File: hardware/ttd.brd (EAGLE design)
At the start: 100 x 80 mm, 19 parts, among them Q1 IRFZ44N, Q2 IRFZ44N, Q3 IRFZ44N, Q4 IRFZ44N, X1 MKDSN1,5/2-5,08, X2 MKDSN1,5/2-5,08

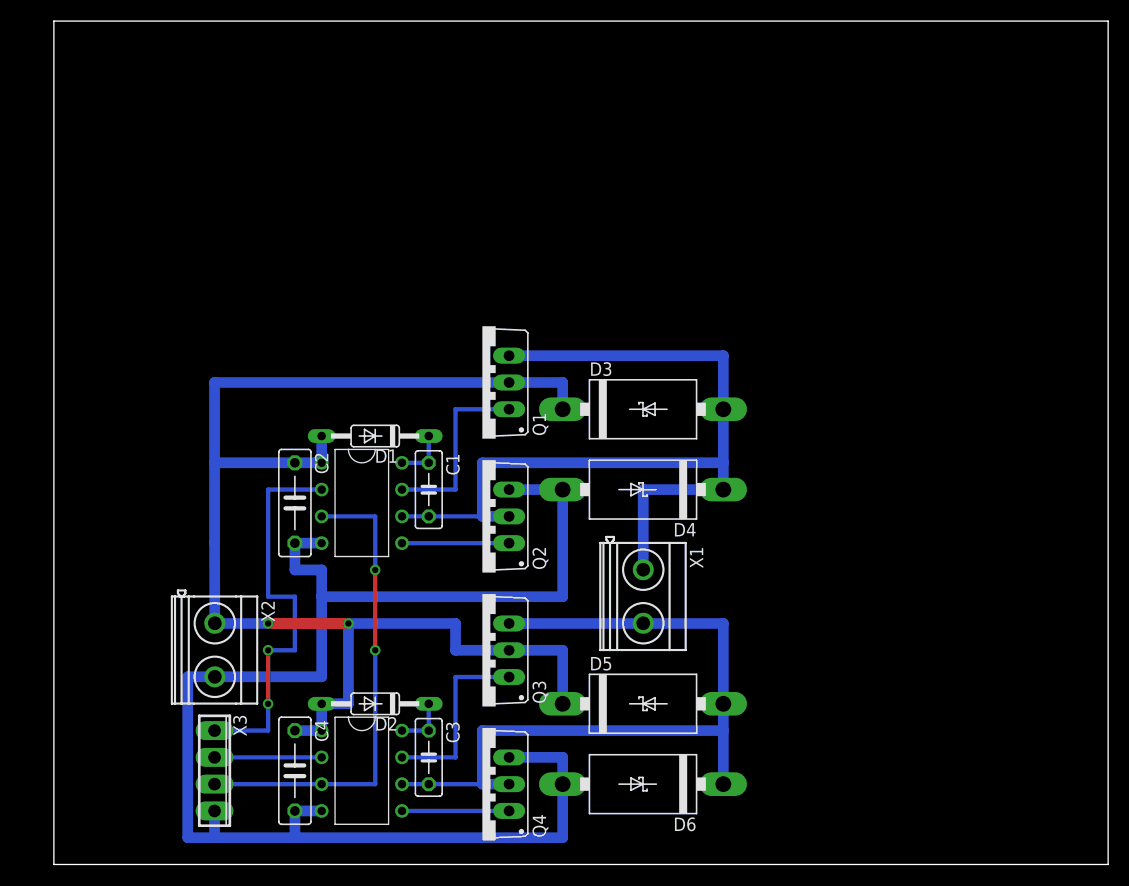
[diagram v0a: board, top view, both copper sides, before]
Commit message: Elektrolytkondensator eingefügt
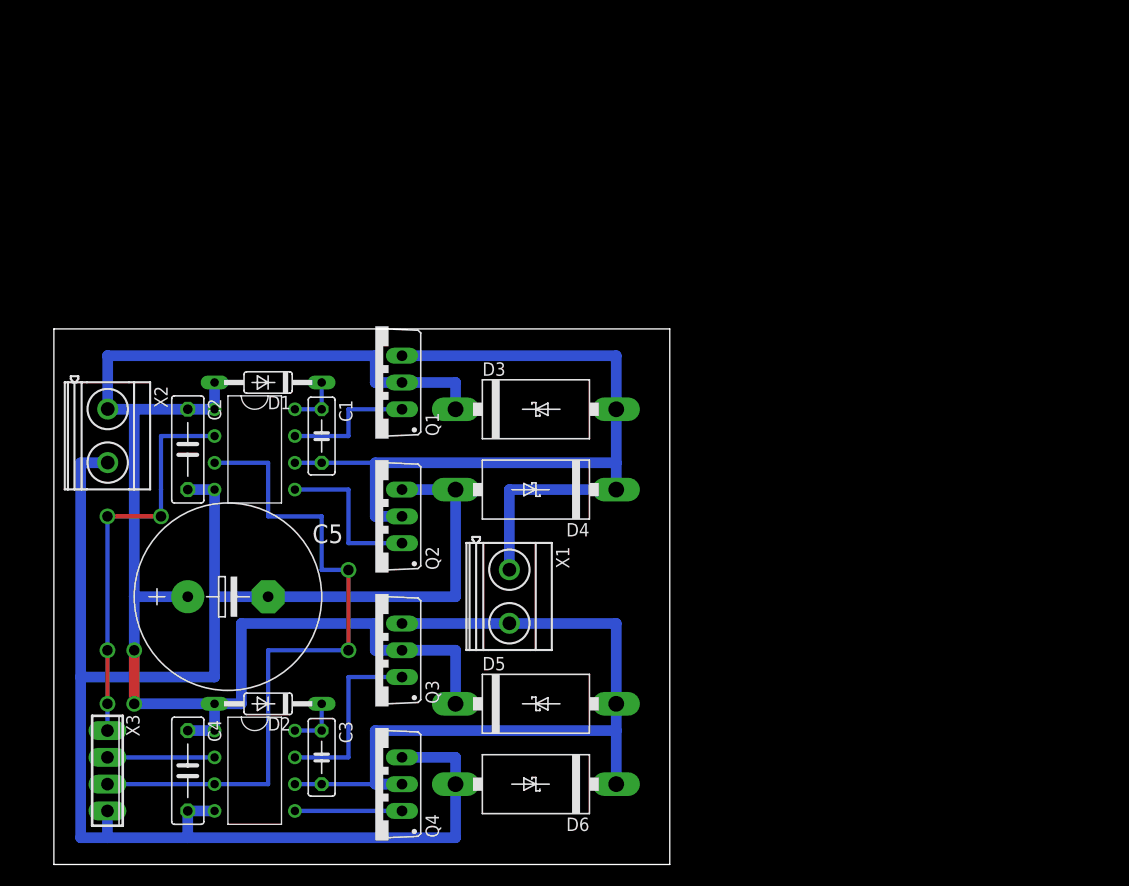
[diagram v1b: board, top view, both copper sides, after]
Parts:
- added C5: (no value), resistor:E7,5-18
- moved X2 22.7 mm to (5.08, 40.6)
- moved X1 12.7 mm to (43.2, 25.4)
- moved C1 11.4 mm to (25.4, 40.6)
- moved C2 11.4 mm to (12.7, 39.4)
- moved D1 11.4 mm to (20.3, 45.7)
- moved U$1 11.4 mm to (19.1, 39.4)
- moved C3 10.2 mm to (25.4, 10.2)
- moved D3 10.2 mm to (45.7, 43.2)
- moved D4 10.2 mm to (45.7, 35.6)
- moved D5 10.2 mm to (45.7, 15.2)
- moved D6 10.2 mm to (45.7, 7.62)
- moved C4 10.2 mm to (12.7, 8.89)
- moved D2 10.2 mm to (20.3, 15.2)
- moved Q1 10.2 mm to (30.5, 45.7)
- moved Q2 10.2 mm to (30.5, 33.0)
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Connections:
- net GND: now also C5.-
- net VIN: now also C5.+
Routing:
- net GND: track 139.7 -> 165.1 mm
- net PWM: track 45.7 -> 66.0 mm
- net VIN: track 127.0 -> 139.7 mm
- net N$1: track 10.2 -> 15.2 mm
- net N$3: track 17.8 -> 12.7 mm
- net N$4: track 86.3 -> 88.9 mm
- net A: vias 2 -> 4
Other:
- board size 100 x 80 mm -> 58.4 x 50.8 mm

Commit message: Transistoren weiter auseinander geschoben für mehr Platz für Kühlkörper
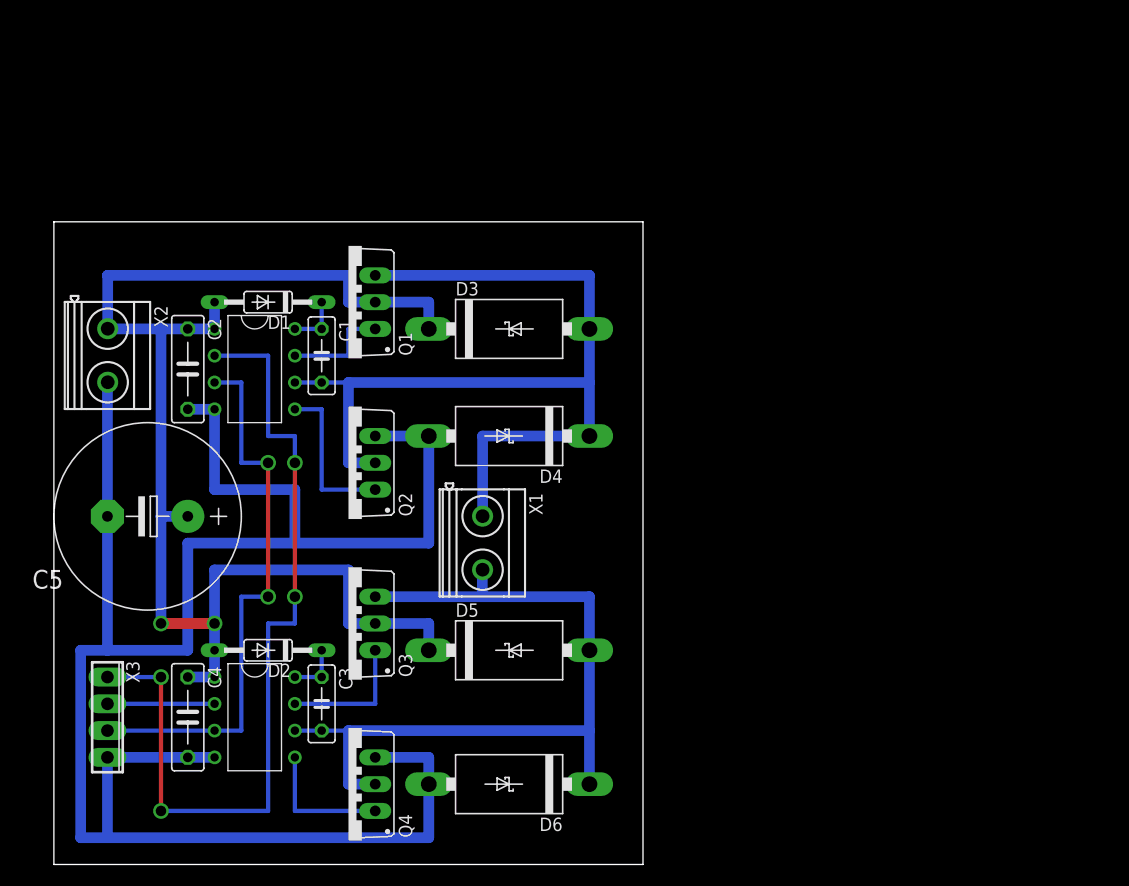
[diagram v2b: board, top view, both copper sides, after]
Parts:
- moved C5 10.8 mm to (8.89, 33.0), turned to 180 degrees
- moved Q1 8.03 mm to (27.9, 53.3)
- moved D3 8.03 mm to (43.2, 50.8)
- moved C2 7.62 mm to (12.7, 47.0)
- moved D1 7.62 mm to (20.3, 53.3)
- moved U$1 7.62 mm to (19.1, 47.0)
- moved C1 7.62 mm to (25.4, 48.3)
- moved X2 7.62 mm to (5.08, 48.3)
- moved X1 5.68 mm to (40.6, 30.5)
- moved D5 5.68 mm to (43.2, 20.3)
- moved D4 5.68 mm to (43.2, 40.6)
- moved Q2 5.68 mm to (27.9, 38.1)
- moved C3 5.08 mm to (25.4, 15.2)
- moved C4 5.08 mm to (12.7, 14.0)
- moved D2 5.08 mm to (20.3, 20.3)
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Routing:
- net A: track 38.1 -> 81.3 mm
- net GND: track 165.1 -> 188.0 mm
- net PWM: track 66.0 -> 53.3 mm
- net VIN: track 139.7 -> 129.5 mm
- net N$8: track 17.8 -> 12.7 mm
- net N$3: track 12.7 -> 10.2 mm
- net N$2: track 10.2 -> 12.7 mm
- net N$7: track 73.7 -> 76.2 mm
- net N$4: track 88.9 -> 91.4 mm
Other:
- board size 58.4 x 50.8 mm -> 55.9 x 61 mm
